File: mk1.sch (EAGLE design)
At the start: 18 parts, among them U1 ATMEGA328P-AU

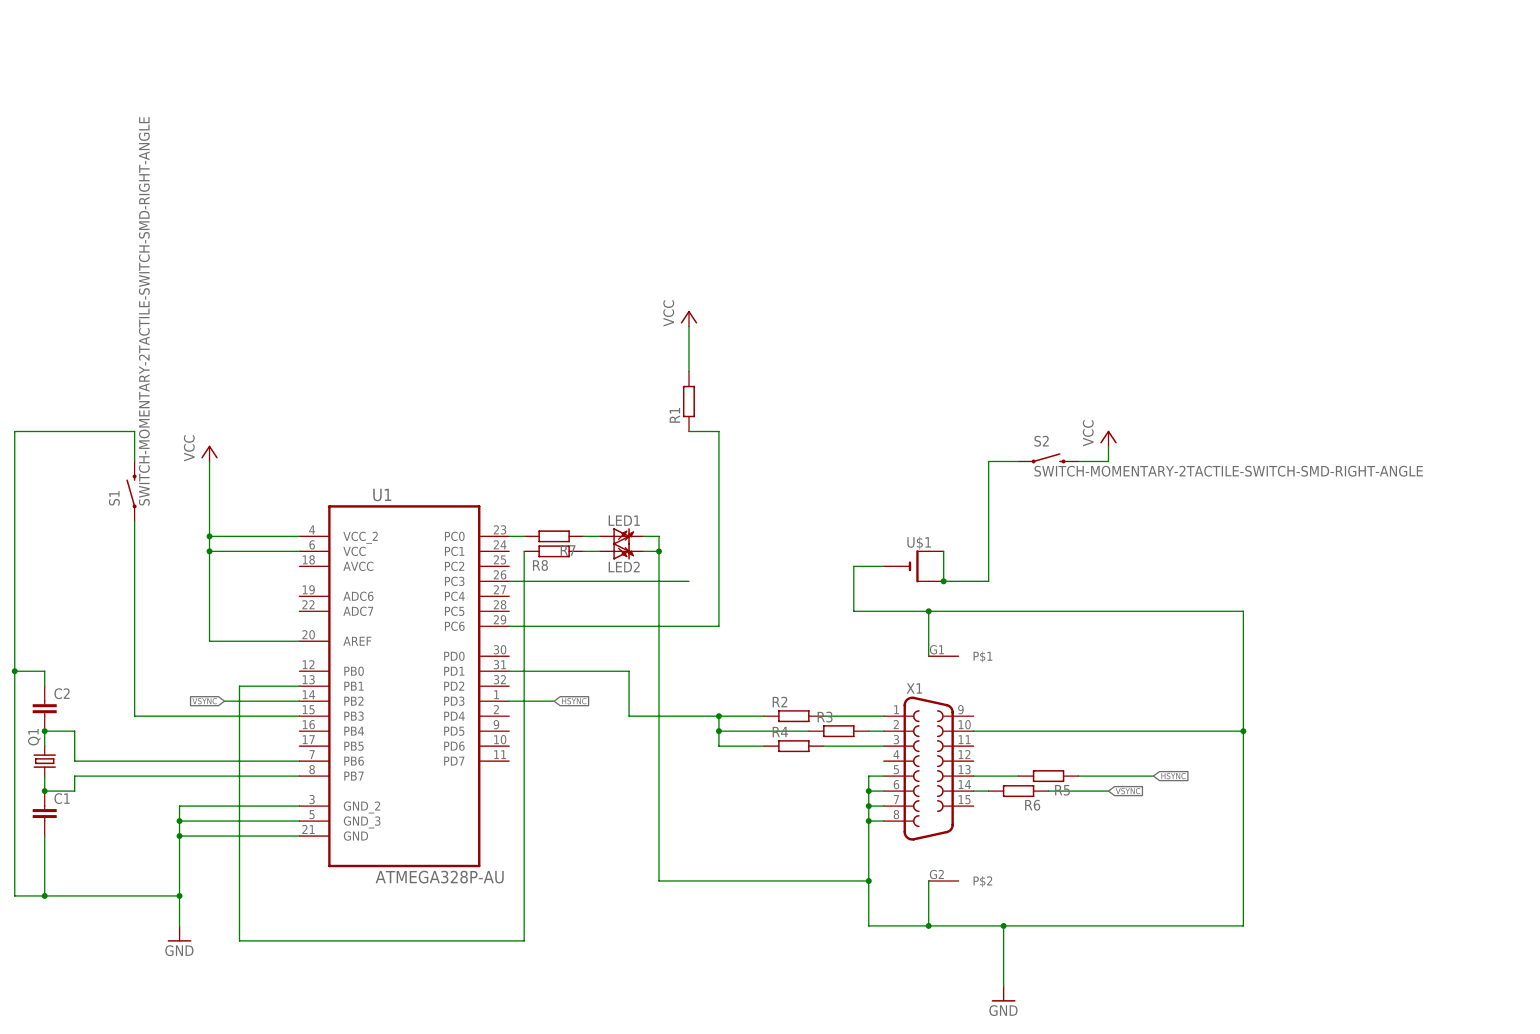
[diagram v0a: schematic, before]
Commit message: Some cleanup. Moved battery holder, less risk of shorting the battery. Changed pins for LEDs for easier routing.
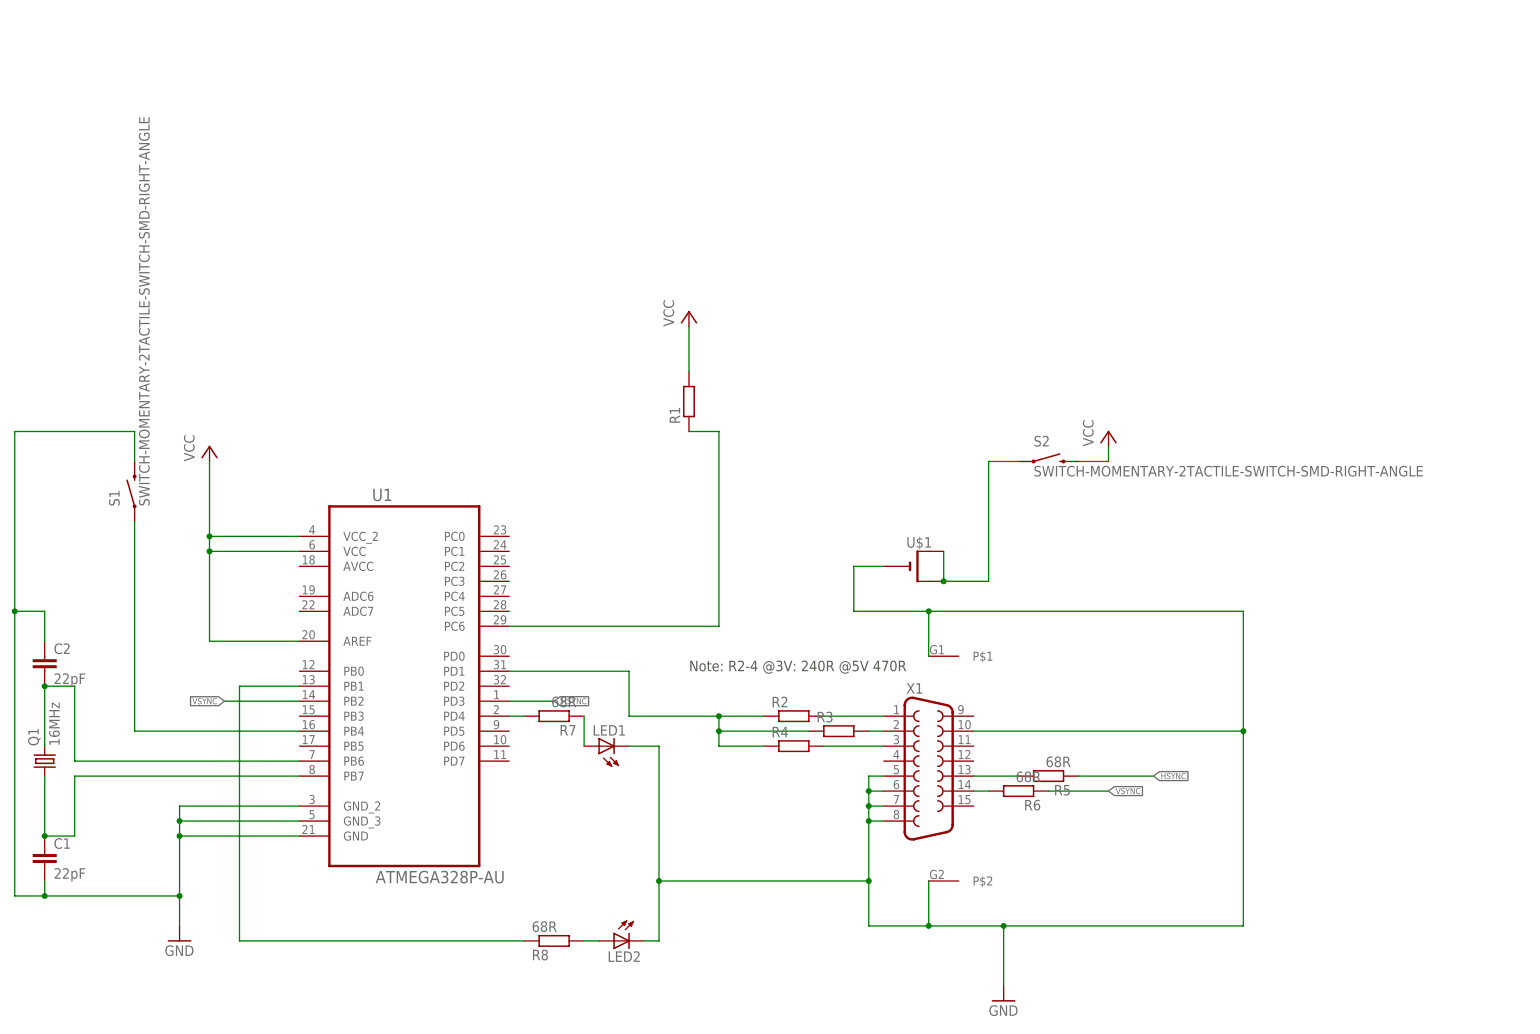
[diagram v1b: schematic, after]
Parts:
- C1, C2: value (none) -> 22pF
- Q1: value (none) -> 16MHz
- R5, R6, R7, R8: value (none) -> 68R
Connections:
- removed net N$14: U1.PC3
- removed net N$5: R7.2, U1.PC0
- new net N$1: R7.2, U1.PD4
- net N$15: now also U1.PB4; no longer U1.PB3
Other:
- note added: "Note: R2-4 @3V: 240R @5V 470R"
- moved on the sheet: C1, C2, LED1, LED2, R7, R8
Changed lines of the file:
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@@
 <?xml version="1.0" encoding="utf-8"?>
 <!DOCTYPE eagle SYSTEM "eagle.dtd">
-<eagle version="8.4.0">
+<eagle version="8.3.1">
 <drawing>
 <settings>
@@
 <part name="U1" library="Atmel_By_element14_Batch_1-00" deviceset="ATMEGA328P-AU" device=""/>
 <part name="GND1" library="supply1" deviceset="GND" device=""/>
-<part name="Q1" library="adafruit" deviceset="CRYSTAL" device="HC49UP"/>
-<part name="C1" library="resistor" deviceset="C-EU" device="C1206"/>
-<part name="C2" library="resistor" deviceset="C-EU" device="C1206"/>
+<part name="Q1" library="adafruit" deviceset="CRYSTAL" device="HC49UP" value="16MHz"/>
+<part name="C1" library="resistor" deviceset="C-EU" device="C1206" value="22pF"/>
+<part name="C2" library="resistor" deviceset="C-EU" device="C1206" value="22pF"/>
 <part name="R1" library="resistor" deviceset="R-EU_" device="M1206"/>
 <part name="X1" library="adafruit" deviceset="F15" device="HDV"/>
@@
 <part name="R3" library="resistor" deviceset="R-EU_" device="M1206"/>
 <part name="R4" library="resistor" deviceset="R-EU_" device="M1206"/>
-<part name="R5" library="resistor" deviceset="R-EU_" device="M1206"/>
-<part name="R6" library="resistor" deviceset="R-EU_" device="M1206"/>
+<part name="R5" library="resistor" deviceset="R-EU_" device="M1206" value="68R"/>
+<part name="R6" library="resistor" deviceset="R-EU_" device="M1206" value="68R"/>
 <part name="GND2" library="supply1" deviceset="GND" device=""/>
 <part name="+3V3" library="supply1" deviceset="VCC" device=""/>
@@
 <part name="+3V1" library="supply1" deviceset="VCC" device=""/>
 <part name="LED1" library="adafruit" deviceset="LED" device="CHIPLED_1206"/>
-<part name="R7" library="resistor" deviceset="R-EU_" device="M1206"/>
-<part name="R8" library="resistor" deviceset="R-EU_" device="M1206"/>
+<part name="R7" library="resistor" deviceset="R-EU_" device="M1206" value="68R"/>
+<part name="R8" library="resistor" deviceset="R-EU_" device="M1206" value="68R"/>
 <part name="LED2" library="adafruit" deviceset="LED" device="CHIPLED_1206"/>
 <part name="S1" library="SparkFun-Electromechanical" deviceset="SWITCH-MOMENTARY-2" device="TACTILE-SWITCH-SMD-RIGHT-ANGLE"/>
@@
 <sheet>
 <plain>
+<text x="124.46" y="53.34" size="1.778" layer="97">Note: R2-4 @3V: 240R @5V 470R</text>
 </plain>
 <instances>
@@
 <instance part="GND1" gate="1" x="38.1" y="7.62"/>
 <instance part="Q1" gate="G$1" x="15.24" y="38.1" rot="R90"/>
-<instance part="C1" gate="G$1" x="15.24" y="30.48"/>
-<instance part="C2" gate="G$1" x="15.24" y="48.26"/>
+<instance part="C1" gate="G$1" x="15.24" y="22.86"/>
+<instance part="C2" gate="G$1" x="15.24" y="55.88"/>
 <instance part="R1" gate="G$1" x="124.46" y="99.06" rot="R90"/>
 <instance part="X1" gate="-1" x="165.1" y="38.1"/>
@@
 <instance part="+3V2" gate="VCC" x="43.18" y="91.44"/>
 <instance part="+3V1" gate="VCC" x="124.46" y="114.3"/>
-<instance part="LED1" gate="G$1" x="111.76" y="76.2" rot="R90"/>
-<instance part="R7" gate="G$1" x="101.6" y="76.2" rot="R180"/>
-<instance part="R8" gate="G$1" x="101.6" y="73.66" rot="MR180"/>
-<instance part="LED2" gate="G$1" x="111.76" y="73.66" rot="MR270"/>
+<instance part="LED1" gate="G$1" x="109.22" y="40.64" rot="R90"/>
+<instance part="R7" gate="G$1" x="101.6" y="45.72" rot="R180"/>
+<instance part="R8" gate="G$1" x="101.6" y="7.62" rot="MR180"/>
+<instance part="LED2" gate="G$1" x="111.76" y="7.62" rot="MR270"/>
 <instance part="S1" gate="G$1" x="30.48" y="83.82" rot="R90"/>
 </instances>
@@
 <wire x1="38.1" y1="30.48" x2="58.42" y2="30.48" width="0.1524" layer="91"/>
 <pinref part="C2" gate="G$1" pin="1"/>
-<wire x1="15.24" y1="50.8" x2="15.24" y2="53.34" width="0.1524" layer="91"/>
-<wire x1="15.24" y1="53.34" x2="10.16" y2="53.34" width="0.1524" layer="91"/>
-<wire x1="10.16" y1="53.34" x2="10.16" y2="15.24" width="0.1524" layer="91"/>
+<wire x1="15.24" y1="58.42" x2="15.24" y2="63.5" width="0.1524" layer="91"/>
+<wire x1="15.24" y1="63.5" x2="10.16" y2="63.5" width="0.1524" layer="91"/>
+<wire x1="10.16" y1="63.5" x2="10.16" y2="15.24" width="0.1524" layer="91"/>
 <wire x1="10.16" y1="15.24" x2="15.24" y2="15.24" width="0.1524" layer="91"/>
 <junction x="38.1" y="15.24"/>
 <pinref part="C1" gate="G$1" pin="2"/>
 <wire x1="15.24" y1="15.24" x2="38.1" y2="15.24" width="0.1524" layer="91"/>
-<wire x1="15.24" y1="25.4" x2="15.24" y2="15.24" width="0.1524" layer="91"/>
+<wire x1="15.24" y1="17.78" x2="15.24" y2="15.24" width="0.1524" layer="91"/>
 <junction x="15.24" y="15.24"/>
 <pinref part="U1" gate="A" pin="GND_3"/>
@@
 <wire x1="30.48" y1="88.9" x2="30.48" y2="93.98" width="0.1524" layer="91"/>
 <wire x1="30.48" y1="93.98" x2="10.16" y2="93.98" width="0.1524" layer="91"/>
-<wire x1="10.16" y1="93.98" x2="10.16" y2="53.34" width="0.1524" layer="91"/>
-<junction x="10.16" y="53.34"/>
+<wire x1="10.16" y1="93.98" x2="10.16" y2="63.5" width="0.1524" layer="91"/>
+<junction x="10.16" y="63.5"/>
 </segment>
 <segment>
@@
 <pinref part="U$1" gate="G$1" pin="-"/>
 <wire x1="157.48" y1="71.12" x2="152.4" y2="71.12" width="0.1524" layer="91"/>
-<pinref part="LED1" gate="G$1" pin="C"/>
-<wire x1="116.84" y1="76.2" x2="119.38" y2="76.2" width="0.1524" layer="91"/>
-<wire x1="119.38" y1="76.2" x2="119.38" y2="73.66" width="0.1524" layer="91"/>
-<wire x1="119.38" y1="73.66" x2="119.38" y2="17.78" width="0.1524" layer="91"/>
+<wire x1="119.38" y1="40.64" x2="119.38" y2="17.78" width="0.1524" layer="91"/>
 <wire x1="119.38" y1="17.78" x2="154.94" y2="17.78" width="0.1524" layer="91"/>
 <junction x="154.94" y="17.78"/>
+<pinref part="LED1" gate="G$1" pin="C"/>
+<wire x1="114.3" y1="40.64" x2="119.38" y2="40.64" width="0.1524" layer="91"/>
 <pinref part="LED2" gate="G$1" pin="C"/>
-<wire x1="116.84" y1="73.66" x2="119.38" y2="73.66" width="0.1524" layer="91"/>
-<junction x="119.38" y="73.66"/>
+<wire x1="116.84" y1="7.62" x2="119.38" y2="7.62" width="0.1524" layer="91"/>
+<wire x1="119.38" y1="7.62" x2="119.38" y2="17.78" width="0.1524" layer="91"/>
+<junction x="119.38" y="17.78"/>
 </segment>
 </net>
@@
 <pinref part="U1" gate="A" pin="PB6"/>
 <wire x1="58.42" y1="38.1" x2="20.32" y2="38.1" width="0.1524" layer="91"/>
-<wire x1="20.32" y1="38.1" x2="20.32" y2="43.18" width="0.1524" layer="91"/>
+<wire x1="20.32" y1="38.1" x2="20.32" y2="50.8" width="0.1524" layer="91"/>
 <pinref part="Q1" gate="G$1" pin="2"/>
-<wire x1="15.24" y1="40.64" x2="15.24" y2="43.18" width="0.1524" layer="91"/>
-<wire x1="15.24" y1="43.18" x2="20.32" y2="43.18" width="0.1524" layer="91"/>
+<wire x1="15.24" y1="40.64" x2="15.24" y2="50.8" width="0.1524" layer="91"/>
+<wire x1="15.24" y1="50.8" x2="20.32" y2="50.8" width="0.1524" layer="91"/>
 <pinref part="C2" gate="G$1" pin="2"/>
-<junction x="15.24" y="43.18"/>
+<junction x="15.24" y="50.8"/>
 </segment>
 </net>
@@
 <wire x1="58.42" y1="35.56" x2="20.32" y2="35.56" width="0.1524" layer="91"/>
 <pinref part="Q1" gate="G$1" pin="1"/>
-<wire x1="15.24" y1="35.56" x2="15.24" y2="33.02" width="0.1524" layer="91"/>
-<wire x1="15.24" y1="33.02" x2="20.32" y2="33.02" width="0.1524" layer="91"/>
-<wire x1="20.32" y1="33.02" x2="20.32" y2="35.56" width="0.1524" layer="91"/>
+<wire x1="15.24" y1="35.56" x2="15.24" y2="25.4" width="0.1524" layer="91"/>
+<wire x1="15.24" y1="25.4" x2="20.32" y2="25.4" width="0.1524" layer="91"/>
+<wire x1="20.32" y1="25.4" x2="20.32" y2="35.56" width="0.1524" layer="91"/>
 <pinref part="C1" gate="G$1" pin="1"/>
-<junction x="15.24" y="33.02"/>
+<junction x="15.24" y="25.4"/>
 </segment>
 </net>
@@
 </segment>
 </net>
-<net name="N$5" class="0">
-<segment>
-<pinref part="U1" gate="A" pin="PC0"/>
-<pinref part="R7" gate="G$1" pin="2"/>
-<wire x1="93.98" y1="76.2" x2="96.52" y2="76.2" width="0.1524" layer="91"/>
-</segment>
-</net>
 <net name="N$6" class="0">
 <segment>
 <pinref part="R7" gate="G$1" pin="1"/>
 <pinref part="LED1" gate="G$1" pin="A"/>
-<wire x1="106.68" y1="76.2" x2="109.22" y2="76.2" width="0.1524" layer="91"/>
+<wire x1="106.68" y1="45.72" x2="106.68" y2="40.64" width="0.1524" layer="91"/>
 </segment>
 </net>
@@
 </segment>
 </net>
-<net name="N$14" class="0">
-<segment>
-<pinref part="U1" gate="A" pin="PC3"/>
-<wire x1="93.98" y1="68.58" x2="124.46" y2="68.58" width="0.1524" layer="91"/>
-</segment>
-</net>
 <net name="N$7" class="0">
 <segment>
 <pinref part="R8" gate="G$1" pin="2"/>
 <pinref part="LED2" gate="G$1" pin="A"/>
-<wire x1="106.68" y1="73.66" x2="109.22" y2="73.66" width="0.1524" layer="91"/>
+<wire x1="106.68" y1="7.62" x2="109.22" y2="7.62" width="0.1524" layer="91"/>
 </segment>
 </net>
 <net name="N$15" class="0">
 <segment>
-<pinref part="U1" gate="A" pin="PB3"/>
-<wire x1="58.42" y1="45.72" x2="30.48" y2="45.72" width="0.1524" layer="91"/>
-<wire x1="30.48" y1="45.72" x2="30.48" y2="78.74" width="0.1524" layer="91"/>
+<wire x1="30.48" y1="43.18" x2="30.48" y2="78.74" width="0.1524" layer="91"/>
 <pinref part="S1" gate="G$1" pin="1"/>
+<pinref part="U1" gate="A" pin="PB4"/>
+<wire x1="58.42" y1="43.18" x2="30.48" y2="43.18" width="0.1524" layer="91"/>
 </segment>
 </net>
 <net name="N$3" class="0">
 <segment>
-<pinref part="R8" gate="G$1" pin="1"/>
-<wire x1="96.52" y1="73.66" x2="96.52" y2="7.62" width="0.1524" layer="91"/>
 <wire x1="96.52" y1="7.62" x2="48.26" y2="7.62" width="0.1524" layer="91"/>
 <pinref part="U1" gate="A" pin="PB1"/>
 <wire x1="48.26" y1="7.62" x2="48.26" y2="50.8" width="0.1524" layer="91"/>
 <wire x1="48.26" y1="50.8" x2="58.42" y2="50.8" width="0.1524" layer="91"/>
+<pinref part="R8" gate="G$1" pin="1"/>
 </segment>
 </net>
@@
 </segment>
 </net>
+<net name="N$1" class="0">
+<segment>
+<pinref part="R7" gate="G$1" pin="2"/>
+<pinref part="U1" gate="A" pin="PD4"/>
+<wire x1="96.52" y1="45.72" x2="93.98" y2="45.72" width="0.1524" layer="91"/>
+</segment>
+</net>
